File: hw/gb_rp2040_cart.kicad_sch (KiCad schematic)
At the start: 13 parts, among them J1 GameBoy_Cartridge, U1 CLXC8T245QRHLRQ1, U2 CLXC8T245QRHLRQ1, U3 CLXC8T245QRHLRQ1, U4 TXU0104

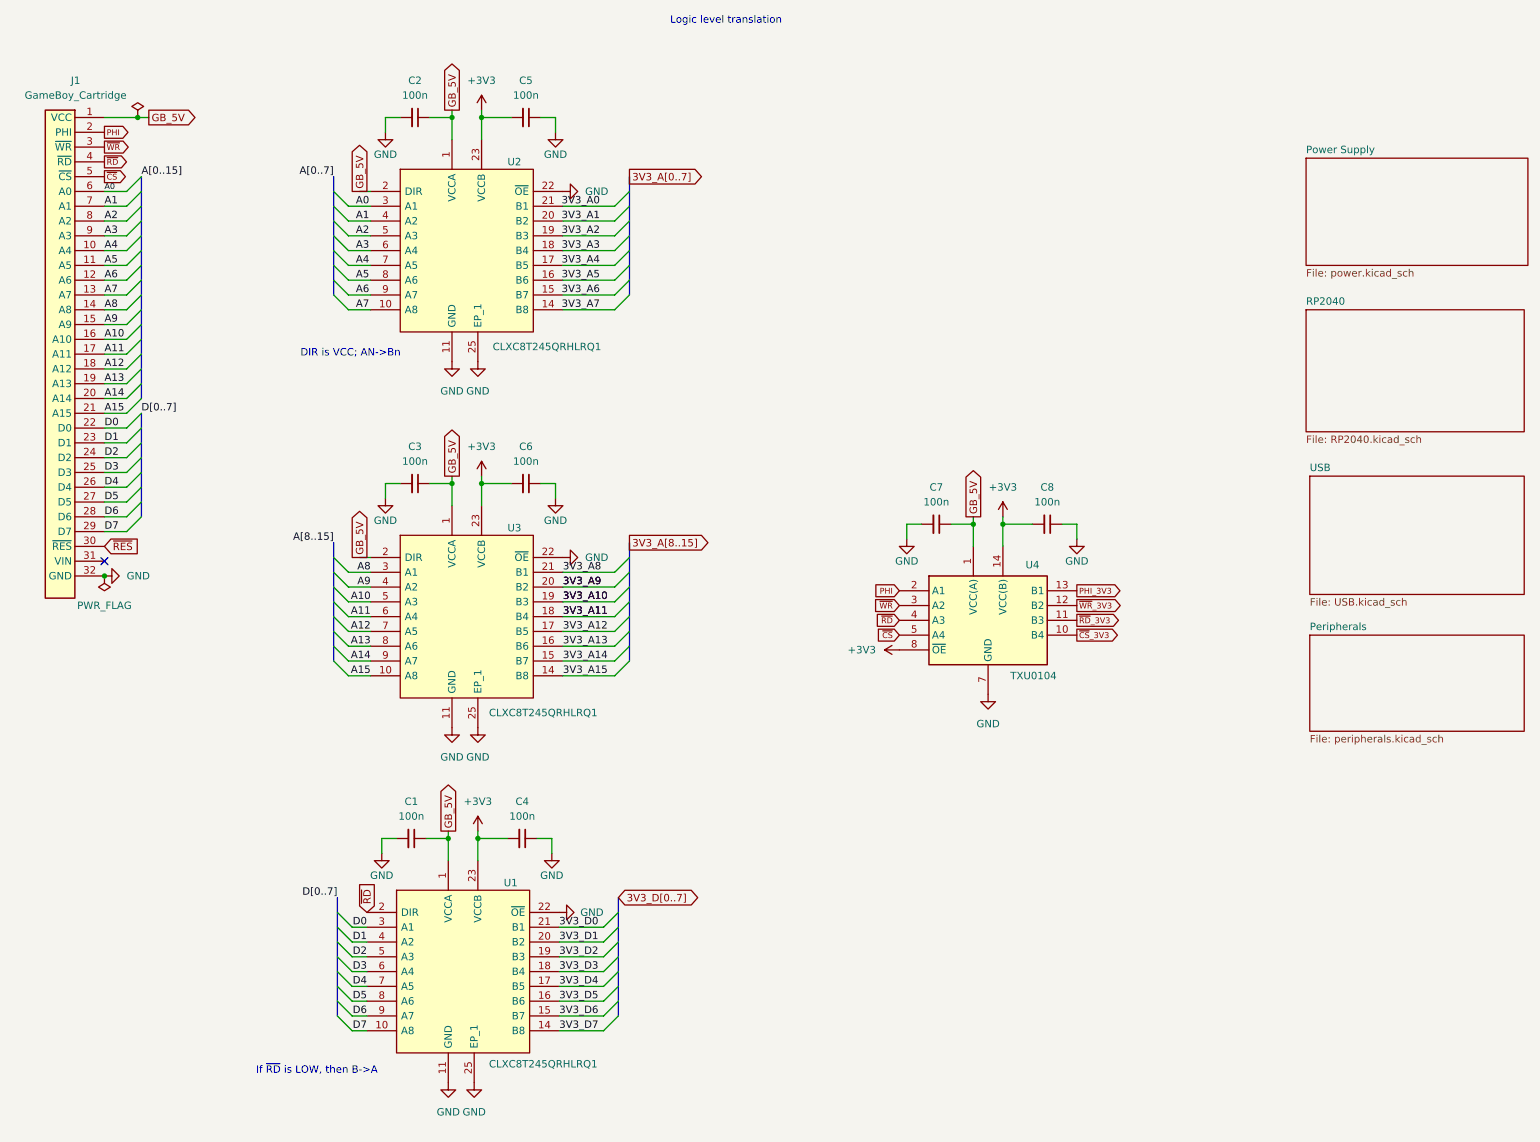
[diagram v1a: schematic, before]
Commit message: hw: use parts from LCSC
Signed-off-by: Mahyar Koshkouei <mk@deltabeard.com>
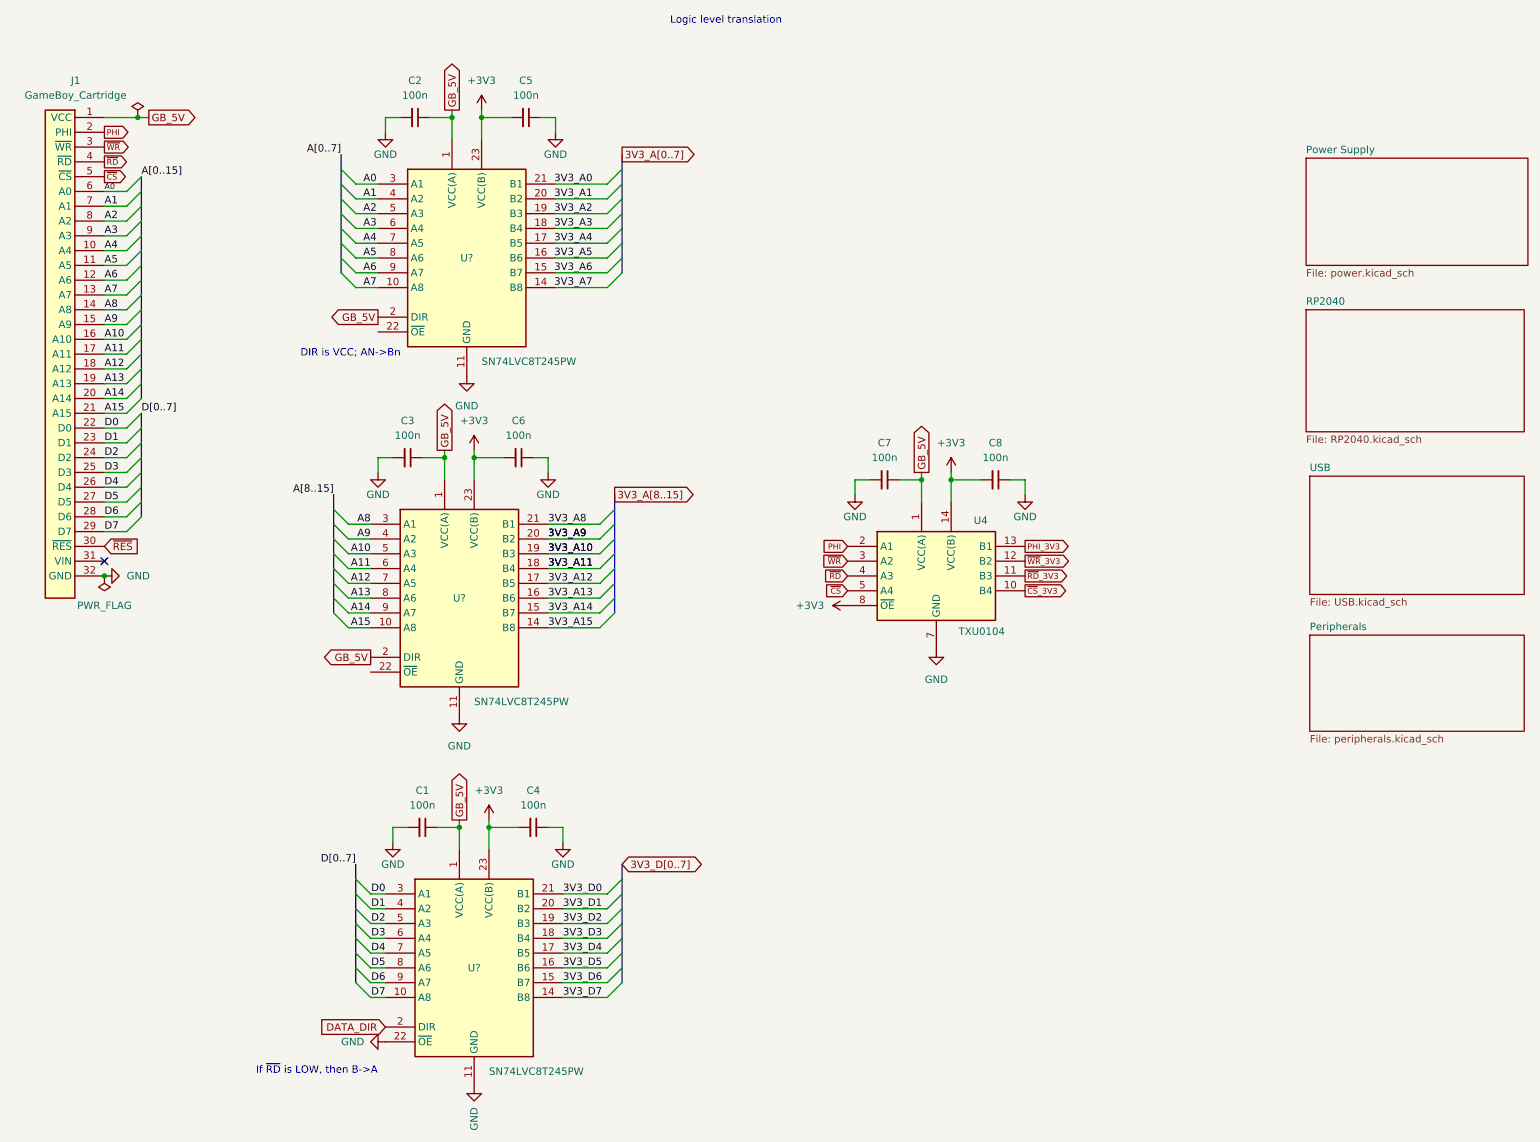
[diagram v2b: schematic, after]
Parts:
- removed U1, U2, U3: CLXC8T245QRHLRQ1, Project_Specific:CLXC8T245QRHLRQ1, symbol Project_specific:CLXC8T245QRHLRQ1
- added U? (x3): SN74LVC8T245PW, Package_SO:TSSOP-24_4.4x7.8mm_P0.65mm, symbol Gekkio_Logic_LevelTranslator:SN74LVC8T245PW
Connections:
- net +3V3: now also U?.23 (VCC(B)), U?.23 (VCC(B)), U?.23 (VCC(B)), U?.24 (VCC(B)), U?.24 (VCC(B)), U?.24 (VCC(B))
- net 3V3_A0: now also U?.21 (B1)
- net 3V3_A1: now also U?.20 (B2)
- net 3V3_A10: now also U?.19 (B3)
- net 3V3_A11: now also U?.18 (B4)
- net 3V3_A12: now also U?.17 (B5)
- net 3V3_A13: now also U?.16 (B6)
- net 3V3_A14: now also U?.15 (B7)
- net 3V3_A15: now also U?.14 (B8)
- net 3V3_A2: now also U?.19 (B3)
- net 3V3_A3: now also U?.18 (B4)
- net 3V3_A4: now also U?.17 (B5)
- net 3V3_A5: now also U?.16 (B6)
- net 3V3_A6: now also U?.15 (B7)
- net 3V3_A7: now also U?.14 (B8)
- net 3V3_A8: now also U?.21 (B1)
- net 3V3_A9: now also U?.20 (B2)
- net 3V3_D0: now also U?.21 (B1)
- net 3V3_D1: now also U?.20 (B2)
- net 3V3_D2: now also U?.19 (B3)
- net 3V3_D3: now also U?.18 (B4)
- net 3V3_D4: now also U?.17 (B5)
- net 3V3_D5: now also U?.16 (B6)
- net 3V3_D6: now also U?.15 (B7)
- net 3V3_D7: now also U?.14 (B8)
- net A0: now also U?.3 (A1)
- net A1: now also U?.4 (A2)
- net A10: now also U?.5 (A3)
- net A11: now also U?.6 (A4)
- net A12: now also U?.7 (A5)
- net A13: now also U?.8 (A6)
- net A14: now also U?.9 (A7)
- net A15: now also U?.10 (A8)
- net A2: now also U?.5 (A3)
- net A3: now also U?.6 (A4)
- net A4: now also U?.7 (A5)
- net A5: now also U?.8 (A6)
- net A6: now also U?.9 (A7)
- net A7: now also U?.10 (A8)
- net A8: now also U?.3 (A1)
- net A9: now also U?.4 (A2)
- net D0: now also U?.3 (A1)
- net D1: now also U?.4 (A2)
- net D2: now also U?.5 (A3)
- net D3: now also U?.6 (A4)
- net D4: now also U?.7 (A5)
- net D5: now also U?.8 (A6)
- net D6: now also U?.9 (A7)
- net D7: now also U?.10 (A8)
- net GB_5V: now also U?.1 (VCC(A)), U?.1 (VCC(A)), U?.1 (VCC(A)), U?.2 (DIR), U?.2 (DIR)
- net GND: now also U?.11 (GND), U?.11 (GND), U?.11 (GND), U?.12 (GND), U?.12 (GND), U?.12 (GND), U?.13 (GND), U?.13 (GND), U?.13 (GND), U?.22 (~{OE})
- new net DATA_DIR: U?.2 (DIR)
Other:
- moved on the sheet: C1, C3, C4, C6, C7, C8, U4

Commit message: hw: complete 2-layer PCB
Signed-off-by: Mahyar Koshkouei <mk@deltabeard.com>
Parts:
- added TP1: TestPoint, TestPoint:TestPoint_Pad_D1.5mm, symbol Connector:TestPoint
- C1: renamed from C3; footprint Capacitor_SMD:C_0603_1608Metric -> Capacitor_SMD:C_0402_1005Metric; LCSC (none) -> C1525
- C2: footprint Capacitor_SMD:C_0603_1608Metric -> Capacitor_SMD:C_0402_1005Metric; LCSC (none) -> C1525
- C3: renamed from C6; footprint Capacitor_SMD:C_0603_1608Metric -> Capacitor_SMD:C_0402_1005Metric; LCSC (none) -> C1525
- C4: renamed from C5; footprint Capacitor_SMD:C_0603_1608Metric -> Capacitor_SMD:C_0402_1005Metric; LCSC (none) -> C1525
- C5: renamed from C7; footprint Capacitor_SMD:C_0603_1608Metric -> Capacitor_SMD:C_0402_1005Metric; LCSC (none) -> C1525
- C6: renamed from C1; footprint Capacitor_SMD:C_0603_1608Metric -> Capacitor_SMD:C_0402_1005Metric; LCSC (none) -> C1525
- C7: renamed from C8; footprint Capacitor_SMD:C_0603_1608Metric -> Capacitor_SMD:C_0402_1005Metric; LCSC (none) -> C1525
- C8: renamed from C4; footprint Capacitor_SMD:C_0603_1608Metric -> Capacitor_SMD:C_0402_1005Metric; LCSC (none) -> C1525
- gave numbers to parts that had none: 3
- renumbered U4 to U3
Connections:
- net GB_5V: now also TP1.1
- net GND: now also U1.22 (~{OE}), U2.22 (~{OE})
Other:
- note added: "If DATA_DIR is LOW, then B->A"
- note removed: "If ~{RD} is LOW, then B->A"
- moved on the sheet: C1, C2, C3, C4, C5, C6, C7, C8, J1, U1, U2, U3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

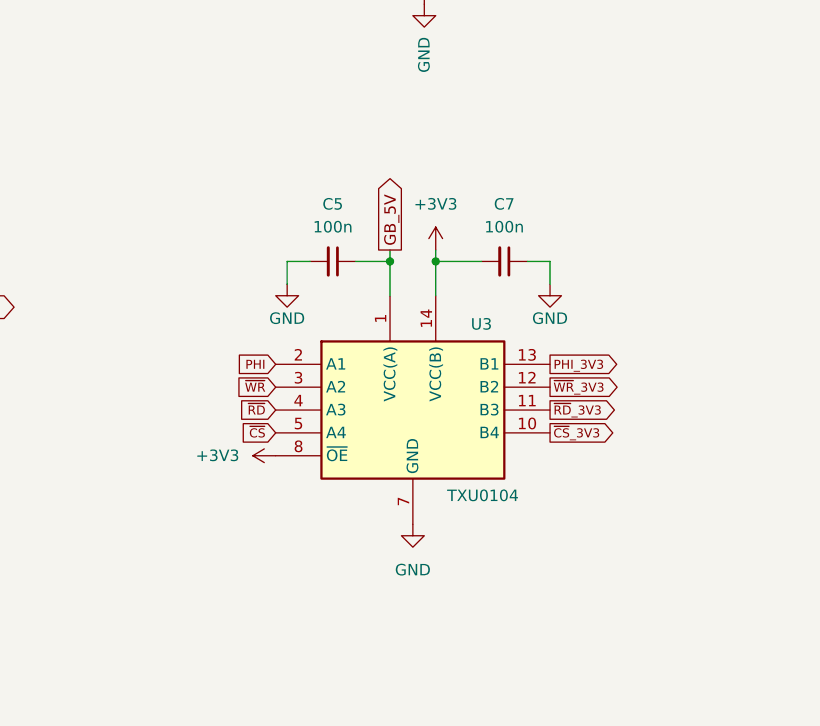
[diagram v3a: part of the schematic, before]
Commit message: hw: replace RTC
Signed-off-by: Mahyar Koshkouei <mk@deltabeard.com>
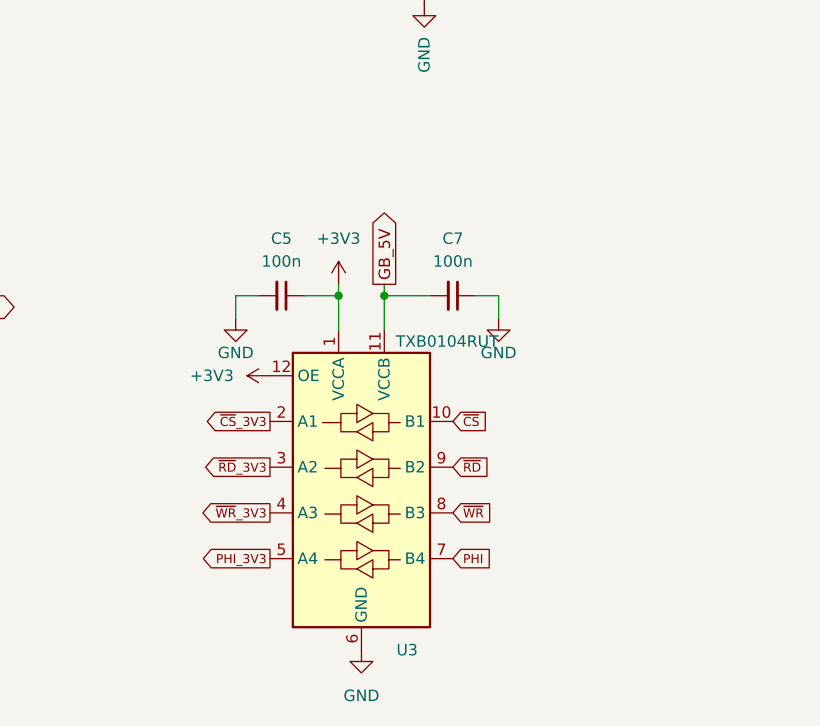
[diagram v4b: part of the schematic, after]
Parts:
- removed U3: TXU0104, Package_SO:TSSOP-14_4.4x5mm_P0.65mm, symbol Project_specific:TXU0104
- added U3: TXB0104RUT, Package_DFN_QFN:Texas_R_PUQFN-N12, symbol Logic_LevelTranslator:TXB0104RUT
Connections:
- net +3V3: now also C5.1, U3.1 (VCCA), U3.12 (OE); no longer C7.2
- net GB_5V: now also C7.2, U3.11 (VCCB); no longer C5.1
- net GND: now also U3.6 (GND)
- net PHI: now also U3.7 (B4)
- net PHI_3V3: now also U3.5 (A4)
- net ~{CS}: now also U3.10 (B1)
- net ~{CS}_3V3: now also U3.2 (A1)
- net ~{RD}: now also U3.9 (B2)
- net ~{RD}_3V3: now also U3.3 (A2)
- net ~{WR}: now also U3.8 (B3)
- net ~{WR}_3V3: now also U3.4 (A3)
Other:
- moved on the sheet: C5, C7

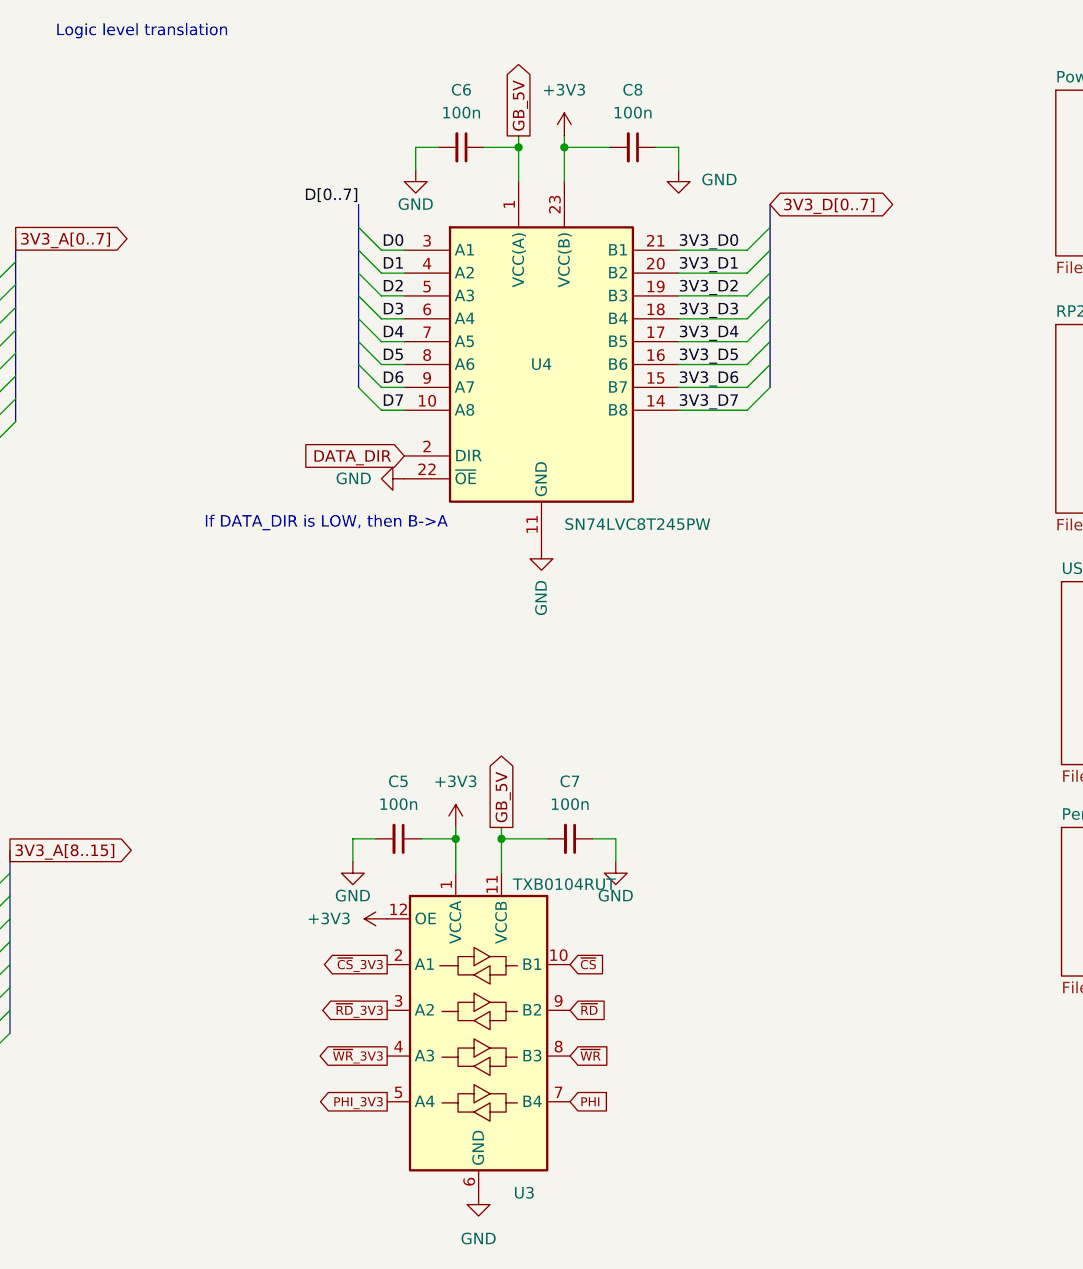
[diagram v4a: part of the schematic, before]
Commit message: hw: complete routing
Use components available on LCSC.

Signed-off-by: Mahyar Koshkouei <mk@deltabeard.com>
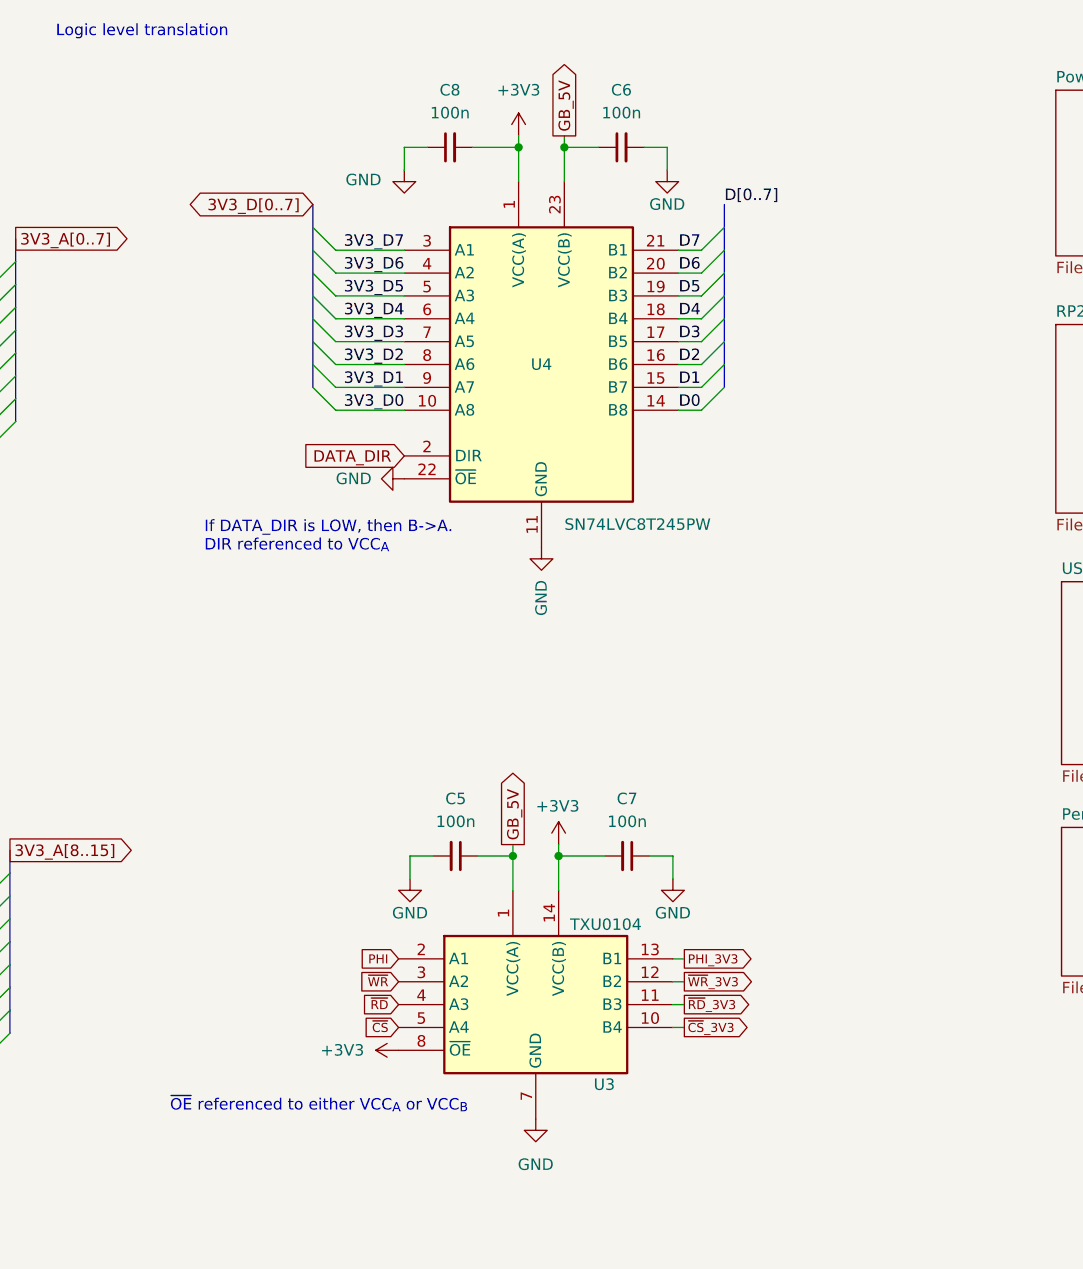
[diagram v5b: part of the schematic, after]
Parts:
- removed U3: TXB0104RUT, Package_DFN_QFN:Texas_R_PUQFN-N12, symbol Logic_LevelTranslator:TXB0104RUT
- added U3: TXU0104, Package_SO:TSSOP-14_4.4x5mm_P0.65mm, symbol Project_specific:TXU0104
- TP1: footprint TestPoint:TestPoint_Pad_D1.5mm -> TestPoint:TestPoint_Pad_D1.0mm
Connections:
- net +3V3: now also C7.2, U4.1 (VCC(A)), U3.14 (VCC(B)), U3.8 (~{OE}); no longer C5.1, U4.23 (VCC(B)), U4.24 (VCC(B))
- net 3V3_D0: now also U4.10 (A8); no longer U4.21 (B1)
- net 3V3_D1: now also U4.9 (A7); no longer U4.20 (B2)
- net 3V3_D2: now also U4.8 (A6); no longer U4.19 (B3)
- net 3V3_D3: now also U4.7 (A5); no longer U4.18 (B4)
- net 3V3_D4: now also U4.6 (A4); no longer U4.17 (B5)
- net 3V3_D5: now also U4.5 (A3); no longer U4.16 (B6)
- net 3V3_D6: now also U4.4 (A2); no longer U4.15 (B7)
- net 3V3_D7: now also U4.3 (A1); no longer U4.14 (B8)
- net D0: now also U4.14 (B8); no longer U4.3 (A1)
- net D1: now also U4.15 (B7); no longer U4.4 (A2)
- net D2: now also U4.16 (B6); no longer U4.5 (A3)
- net D3: now also U4.17 (B5); no longer U4.6 (A4)
- net D4: now also U4.18 (B4); no longer U4.7 (A5)
- net D5: now also U4.19 (B3); no longer U4.8 (A6)
- net D6: now also U4.20 (B2); no longer U4.9 (A7)
- net D7: now also U4.21 (B1); no longer U4.10 (A8)
- net GB_5V: now also C5.1, U4.23 (VCC(B)), U4.24 (VCC(B)), U3.1 (VCC(A)); no longer C7.2, U4.1 (VCC(A))
- net GND: now also U3.7 (GND)
- net PHI: now also U3.2 (A1)
- net PHI_3V3: now also U3.13 (B1)
- net ~{CS}: now also U3.5 (A4)
- net ~{CS}_3V3: now also U3.10 (B4)
- net ~{RD}: now also U3.4 (A3)
- net ~{RD}_3V3: now also U3.11 (B3)
- net ~{WR}: now also U3.3 (A2)
- net ~{WR}_3V3: now also U3.12 (B2)
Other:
- note added: "If DATA_DIR is LOW, then B->A. DIR referenced to VCC_{A}"
- note added: "~{OE} referenced to either VCC_{A} or VCC_{B}"
- note removed: "If DATA_DIR is LOW, then B->A"
- moved on the sheet: C5, C6, C7, C8
